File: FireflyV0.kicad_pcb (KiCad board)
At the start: 2 copper layers, 63.2 x 43.1 mm, 21 parts, among them J1 USB4125-GF-A-0190, J2 USB4125-GF-A-0190, J3 USB4125-GF-A-0190, J4 Conn_01x04, J5 Conn_01x03, U1 PEC12R-4215F-S0024, U2 Pico

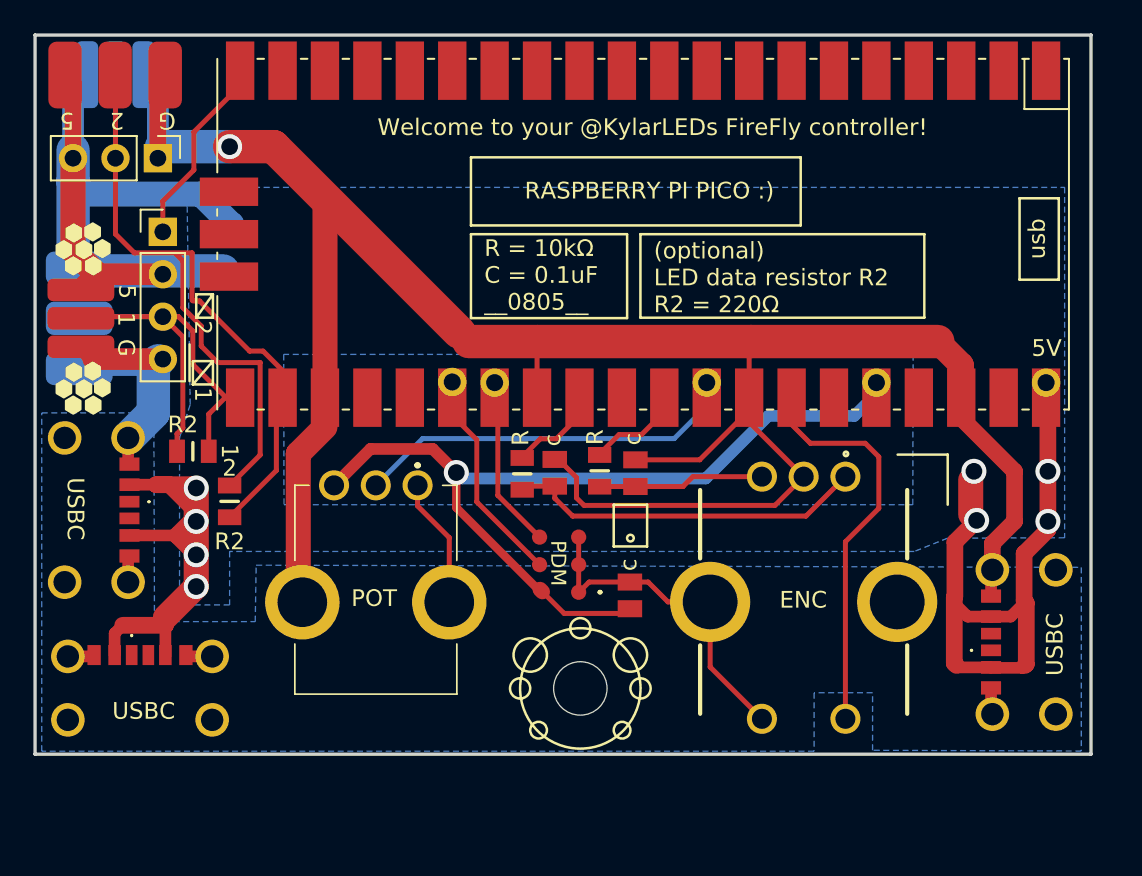
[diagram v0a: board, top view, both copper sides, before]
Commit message: Adding puttons
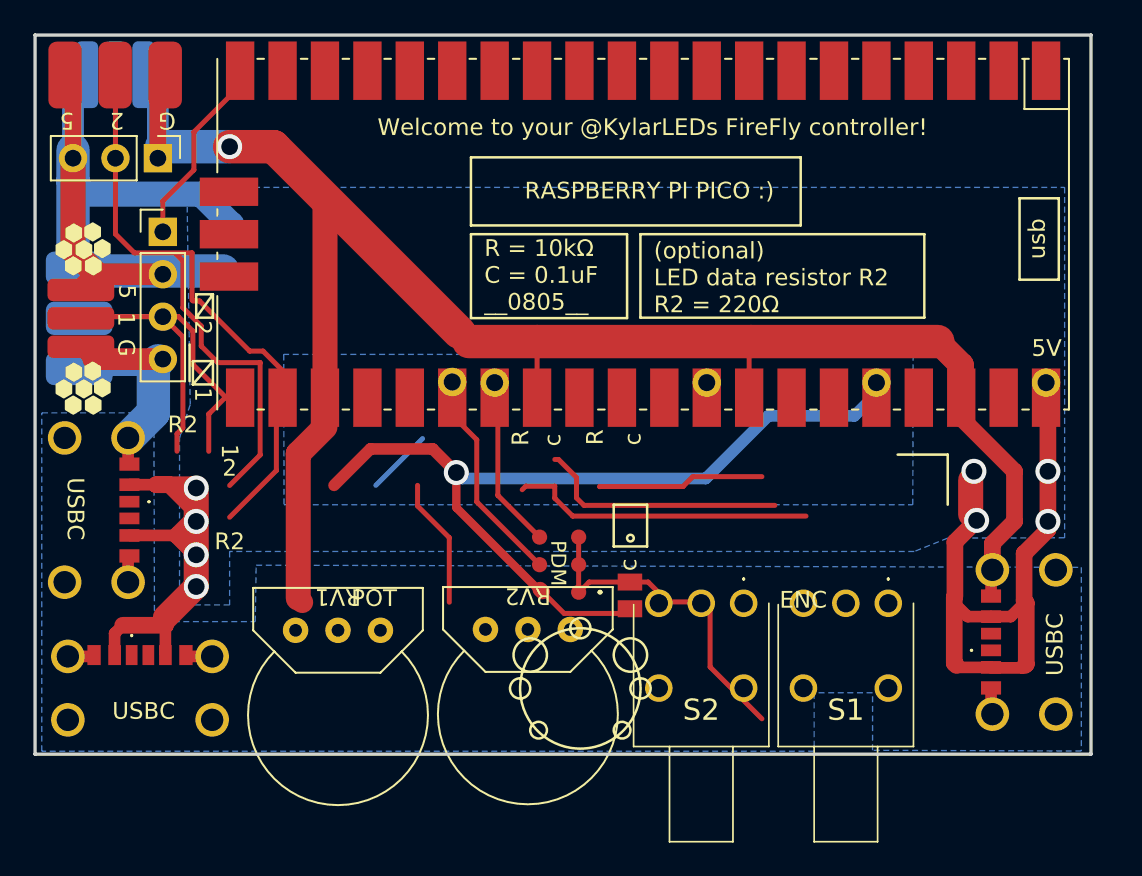
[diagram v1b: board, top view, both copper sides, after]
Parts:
- removed C1, C2: C0805C104M5RAC, SamacSys_Parts:CAPC2012X88N
- removed R** (x2): RESC2012X60N, SamacSys_Parts:RESC2012X60N
- removed R1, R2: RC0805JR-071M6L, SamacSys_Parts:RESC2012X60N
- removed REF**: MountingHole_3.2mm_M3_ISO7380, MountingHole:MountingHole_3.2mm_M3_ISO7380
- removed U1: PEC12R-4215F-S0024, SamacSys_Parts:PEC12R-4XXXF-SXXXX_court
- removed VR1: PTV09A-4020F-B104, SamacSys_Parts:PTV09A4020FB103
- added RV1: R_Potentiometer, Varistor:3352T-1-104LF, F.Cu at (31.5, 48.5)
- added RV2: R_Potentiometer, Varistor:3352T-1-104LF, F.Cu at (42.9, 48.5)
- added S1: TP32W008000, SamacSys_Parts:TP32W008000, F.Cu at (64.4, 46.9)
- added S2: TP32W008000, SamacSys_Parts:TP32W008000, F.Cu at (55.8, 46.9)
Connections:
- U2 pad 29: ENC_A -> unconnected-(U2-Pad29)
- U2 pad 31: ENC_B -> POT2_ADC
- U2 pad 32: POT_ADC -> POT1_ADC
- U2 pad 34: ENC_SW -> unconnected-(U2-Pad34)
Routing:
- net (no net): track 0.00 -> 28.2 mm
- net ENC_SW: track 25.0 -> 0.00 mm
- net POT_ADC: track 23.2 -> 0.00 mm
- net /A: track 21.6 -> 0.00 mm
- net GND: track 198.3 -> 183.2 mm
- net /B: track 9.96 -> 0.00 mm
- net ENC_B: track 6.59 -> 0.00 mm
- net ENC_A: track 6.49 -> 0.00 mm
- net POT1_ADC: track 0.00 -> 3.96 mm

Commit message: Finished traces and vias, only planes and silkscreen to go
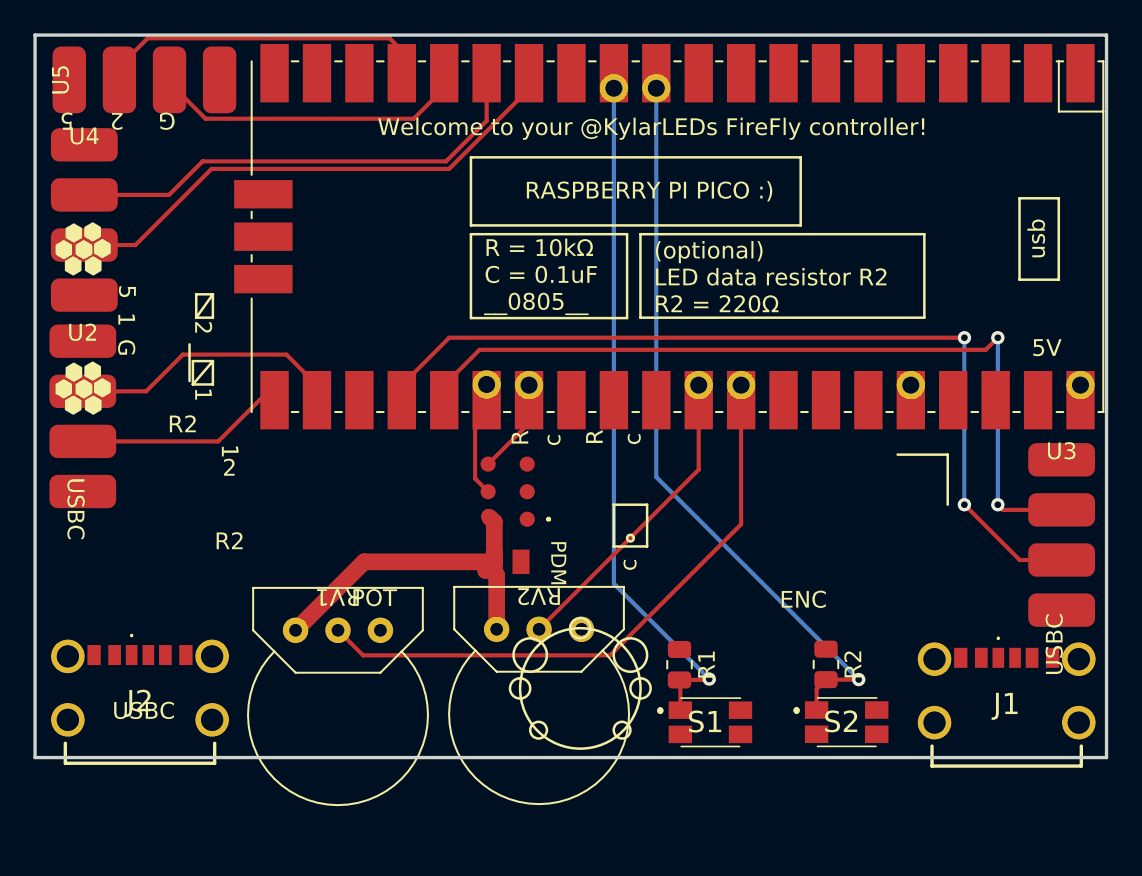
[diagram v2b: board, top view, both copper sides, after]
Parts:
- removed J3: USB4125-GF-A-0190, SamacSys_Parts:USB4125GFA0190_nosilk
- removed J4: Conn_01x04, Connector_PinHeader_2.54mm:PinHeader_1x04_P2.54mm_Vertical
- removed J5: Conn_01x03, Connector_PinHeader_2.54mm:PinHeader_1x03_P2.54mm_Vertical
- removed LEDS1, LEDS3: ledstrip_3pin_5mm, kylarLEDs:ledstrip_3pin_5mm
- removed LEDS2, LEDS4: ledstrip_3pin_10mm, kylarLEDs:ledstrip_3pin_10mm
- added R1: R_US, Resistor_SMD:R_0805_2012Metric, F.Cu at (51.9, 50.6)
- added R2: R_US, Resistor_SMD:R_0805_2012Metric, F.Cu at (60.7, 50.6)
- added U2: LEDS4, SamacSys_Parts:LEDS4, F.Cu at (16.2, 31.2)
- added U3: LEDS4, SamacSys_Parts:LEDS4, F.Cu at (74.8, 38.3)
- added U4: LEDS4, SamacSys_Parts:LEDS4, F.Cu at (16.3, 19.4)
- added U5: LEDS4, SamacSys_Parts:LEDS4, F.Cu at (15.4, 15.6)
- J1, J2: footprint SamacSys_Parts:USB4125GFA0190_nosilk -> SamacSys_Parts:USB4125GFA0190
- S1, S2: value TP32W008000 -> EVQ-P7J01P; footprint SamacSys_Parts:TP32W008000 -> SamacSys_Parts:EVQP7J01P
- moved J1 56.9 mm to (71.5, 53.2), turned to 0 degrees
- moved S1 13.1 mm to (53.5, 54.0), turned to 0 degrees
- moved S2 9.23 mm to (61.6, 54.0), turned to 0 degrees
- moved C3 7.59 mm to (41.6, 44.4), turned to 0 degrees
- moved MK1 5.35 mm to (41.6, 40.2)
- moved U1 2.07 mm to (51.8, 24.9)
- moved RV2 0.67 mm to (43.5, 48.5)
- renumbered U2 to U1
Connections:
- S1 pad 1: unconnected-(S1-Pad1) -> BTN_1
- S1 pad 3: unconnected-(S1-Pad3) -> GND
- S2 pad 1: unconnected-(S2-Pad1) -> BTN_2
- S2 pad 3: unconnected-(S2-Pad3) -> GND
- U1 pad 11: unconnected-(U2-Pad11) -> BTN_2
- U1 pad 12: unconnected-(U2-Pad12) -> BTN_1
- U1 pad 14: unconnected-(U2-Pad14) -> LED_DATA_3
- U1 pad 15: unconnected-(U2-Pad15) -> LED_CLK_3
- U1 pad 16: unconnected-(U2-Pad16) -> LED_DATA_4
- U1 pad 17: unconnected-(U2-Pad17) -> LED_CLK_4
- U1 pad 20: APA_1 -> unconnected-(U1-Pad20)
- U1 pad 22: LED_DATA_2 -> LED_CLK_1
- U1 pad 24: unconnected-(U2-Pad24) -> LED_DATA_2
- U1 pad 25: unconnected-(U2-Pad25) -> LED_CLK_2
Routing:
- net GND: track 183.2 -> 0.00 mm, vias 1 -> 0
- net 5V: track 117.8 -> 0.00 mm, vias 8 -> 0
- net LED_CLK_2: track 0.00 -> 48.3 mm, vias 0 -> 2
- net BTN_2: track 0.00 -> 44.4 mm, vias 0 -> 1
- net BTN_1: track 0.00 -> 41.4 mm, vias 0 -> 1
- net POT1_ADC: track 3.96 -> 36.3 mm
- net 3V3: track 52.1 -> 21.0 mm, vias 1 -> 0
- net LED_DATA_3: track 0.00 -> 30.5 mm
- net (no net): track 28.2 -> 0.00 mm
- net LED_CLK_3: track 0.00 -> 27.9 mm
- net LED_CLK_4: track 0.00 -> 21.0 mm
- net POT2_ADC: track 0.00 -> 18.6 mm
- net LED_DATA_4: track 0.00 -> 18.3 mm
- net LED_DATA_1: track 29.6 -> 12.9 mm
- net LED_CLK_1: track 0.00 -> 15.7 mm
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- removed copper zone on B.Cu, net 5V
- removed copper zone on B.Cu, net GND
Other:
- board size 63.2 x 43.1 mm -> 64.2 x 43.3 mm

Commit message: Done minus accelerometer
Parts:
- moved R2 1.45 mm to (59.6, 49.6)
- moved R1 0.92 mm to (51.9, 49.7)
- moved S2 0.50 mm to (61.1, 54.0)
- moved C3 0.31 mm to (41.8, 44.7)
- moved S1 0.08 mm to (53.4, 54.0)
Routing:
- net GND: track 0.00 -> 96.2 mm, vias 0 -> 4
- net 3V3: track 21.0 -> 70.0 mm
- net 5V: track 0.00 -> 4.26 mm
- net BTN_1: track 41.4 -> 41.9 mm
- added copper zone on F.Cu, net 5V
- added copper zone on B.Cu, net GND
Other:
- board text added: "C1"
- board text added: "C2"
- board text added: "C3"
- board text added: "D1"
- board text added: "D2"
- board text added: "D3"
- board text added: "D4"
- board text added: "clk_1 =gp17 data_1=gp16 clk_2 =gp19 data_2=gp18"
- board text added: "pot_1 =gp27 pot_2 =gp26"
- board text removed: "1"
- board text removed: "2"
- board text removed: "ENC"
- board text removed: "POT"
- board text removed: "R"
- board text removed: "R2"
- board text removed: "USBC"
- board text removed: "enc_a =gp22 enc_b =gp26 enc_sw=gp28"
- board text removed: "pdm_clk =gp21 pdm_dat =gp20 pot_adc1=gp27"

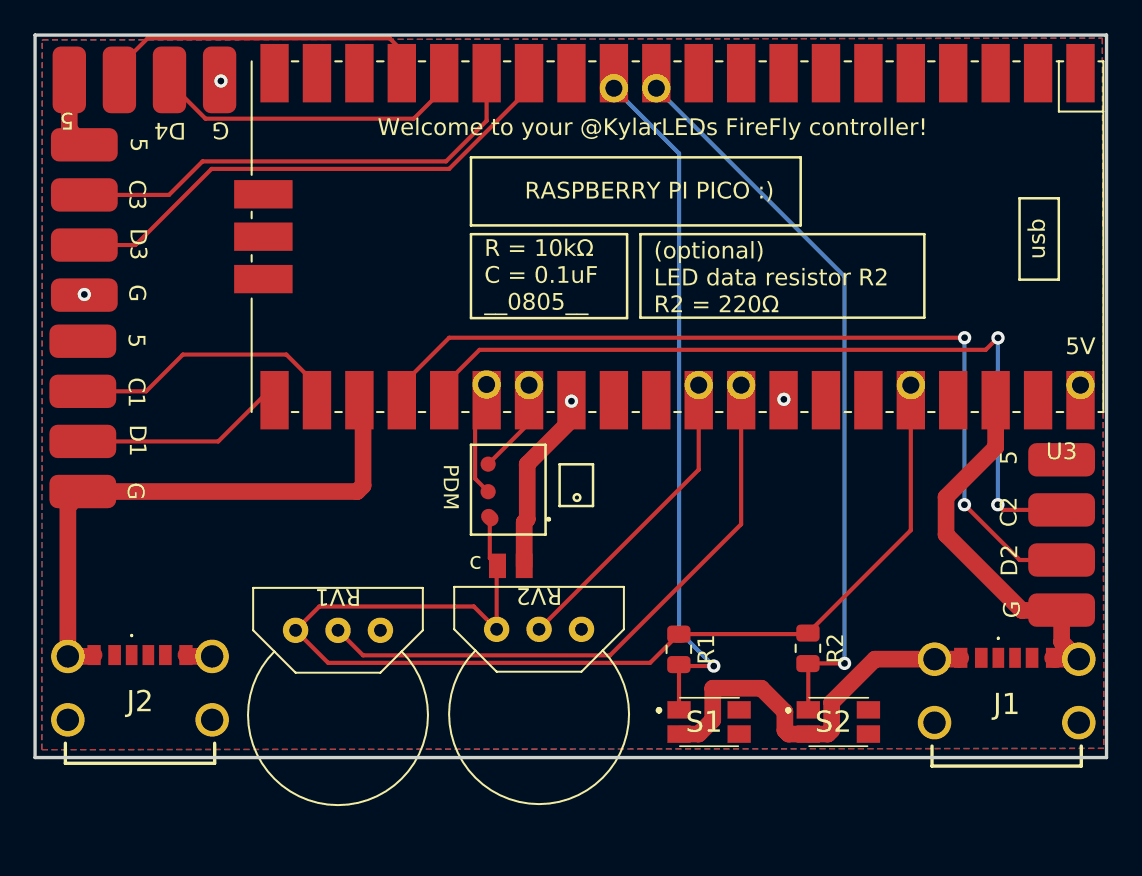
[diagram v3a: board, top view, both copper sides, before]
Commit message: Adding bom, switching switch
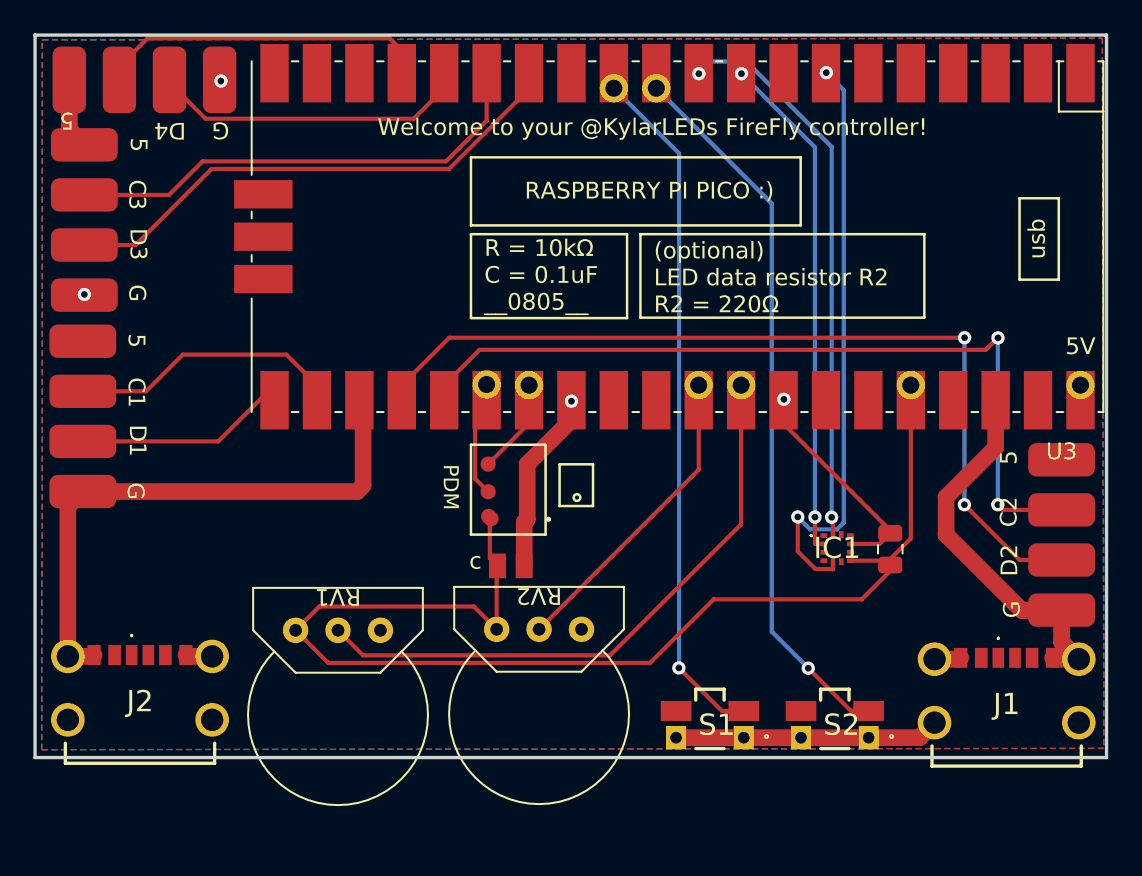
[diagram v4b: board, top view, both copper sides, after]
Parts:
- removed R1, R2: R_US, Resistor_SMD:R_0805_2012Metric
- added C1: C0805C104M5RAC, Capacitor_SMD:C_0805_2012Metric, F.Cu at (64.6, 43.7)
- added IC1: MXC6655XA, SamacSys_Parts:MXC6655XA, F.Cu at (61.4, 43.6)
- S1, S2: value EVQ-P7J01P -> EVQ-9P701P; footprint SamacSys_Parts:EVQP7J01P -> SamacSys_Parts:EVQ-9P701P
- moved S1 0.38 mm to (53.8, 54.1), turned to 180 degrees
- moved S2 0.17 mm to (61.2, 54.1), turned to 180 degrees
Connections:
- S1 pad 1: BTN_1 -> GND
- S1 pad 2: unconnected-(S1-Pad2) -> BTN_1
- S1 pad 3: GND -> unconnected-(S1-Pad3)
- S1 pad 4: unconnected-(S1-Pad4) -> GND
- S2 pad 1: BTN_2 -> GND
- S2 pad 2: unconnected-(S2-Pad2) -> BTN_2
- S2 pad 3: GND -> unconnected-(S2-Pad3)
- S2 pad 4: unconnected-(S2-Pad4) -> GND
- U1 pad 10: unconnected-(U1-Pad10) -> ACC_CLK
- U1 pad 7: unconnected-(U1-Pad7) -> ACC_INT
- U1 pad 9: unconnected-(U1-Pad9) -> ACC_DATA
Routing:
- net ACC_INT: track 0.00 -> 35.7 mm, vias 0 -> 2
- net ACC_CLK: track 0.00 -> 33.6 mm, vias 0 -> 2
- net ACC_DATA: track 0.00 -> 30.5 mm, vias 0 -> 2
- net GND: track 96.2 -> 104.2 mm
- net 3V3: track 70.0 -> 73.3 mm
- net BTN_2: track 44.1 -> 43.2 mm
- net BTN_1: track 41.9 -> 41.3 mm
